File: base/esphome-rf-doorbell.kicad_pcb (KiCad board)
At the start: 2 copper layers, 65 x 54.7 mm, 100 parts, among them J1 B4B-XH, J2 CONUFL001-SMD-T, J3 Conn_01x01, J4 Conn_01x01, SW1 Boot, U1 BQ25628E, U2 RFM69W, U3 TPS7A2033, U4 MAX17261xxTD, U5 TPS629206DRLR, U6 G3VM-31DR, U7 ESP32-S2-MINI-2, U8 G3VM-63ER, U9 TLP2391

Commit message: Base board Rev3
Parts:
- removed the C1 at (130.3, 77.9)
- removed the C2 at (127.9, 77.7)
- removed C21: 0.1uF, Capacitor_SMD:C_0402_1005Metric
- removed C23: 1uF 50V, Capacitor_SMD:C_0805_2012Metric
- removed the C3 at (124.3, 81.1)
- removed the C4 at (131.6, 80.6)
- removed the C5 at (130.3, 80.2)
- removed the D3 at (114.9, 80.8)
- removed the D4 at (114.8, 78.2)
- removed J3, J4: Conn_01x01, TestPoint:TestPoint_Keystone_5000-5004_Miniature
- removed the JP1 at (118.2, 80.8)
- removed the JP2 at (118.2, 78.2)
- removed L2: 2.2uH, Inductor_SMD:L_1210_3225Metric
- removed the R1 at (111.4, 80.8)
- removed the R10 at (137.3, 96.1)
- removed the R2 at (111.4, 78.2)
- removed the R20 at (158.2, 96.9)
- removed the R21 at (158.2, 99.9)
- removed the R4 at (125.4, 94.1)
- removed the REF** at (139.5, 109.5)
- removed the REF** at (117.4, 72.1)
- removed the RV1 at (116.0, 72.9)
- removed the TP1 at (122.6, 72.9)
- removed TP11: TestPoint, TestPoint:TestPoint_Pad_D1.5mm
- removed the TP4 at (123.2, 86.9)
- removed the TP5 at (111.1, 72.9)
- removed the U7 at (125.2, 115.6)
- removed kibuzzard-691E1EB0: G***, kibuzzard-691E1EB0
- removed kibuzzard-691E1EB7: G***, kibuzzard-691E1EB7
- removed kibuzzard-691E1ECB: G***, kibuzzard-691E1ECB
- removed kibuzzard-691E1ED6: G***, kibuzzard-691E1ED6
- added C16: 1uF, Capacitor_SMD:C_0402_1005Metric, F.Cu at (138.4, 112.4)
- added C19: 1uF, Capacitor_SMD:C_0402_1005Metric, F.Cu at (148.9, 112.8)
- added C8: 47uF, Capacitor_SMD:C_0805_2012Metric, F.Cu at (132.9, 120.2)
- added D5: Red, LED_SMD:LED_0603_1608Metric, F.Cu at (142.0, 120.1)
- added JP4: SolderJumper_2_Open, Jumper:SolderJumper-2_P1.3mm_Open_RoundedPad1.0x1.5mm, F.Cu at (142.6, 117.3)
- added Q1: PMZB390UNE, Package_DFN_QFN:Diodes_DFN1006-3, F.Cu at (127.2, 106.0)
- added R12: 1.27M, Resistor_SMD:R_0402_1005Metric, F.Cu at (137.0, 112.9)
- added R16: 1k, Resistor_SMD:R_0402_1005Metric, F.Cu at (143.3, 106.6)
- added R17: 1k, Resistor_SMD:R_0402_1005Metric, F.Cu at (143.3, 113.4)
- added R18: 1k, Resistor_SMD:R_0402_1005Metric, F.Cu at (143.4, 120.1)
- added R8: 47k, Resistor_SMD:R_0402_1005Metric, F.Cu at (134.5, 106.5)
- added REF**: KiCad-Logo2_6mm_SilkScreen, Symbol:KiCad-Logo2_6mm_SilkScreen, B.Cu at (118.7, 113.4)
- added SW2: CL-SB-22A-11T, lib:CL-SB-22A, F.Cu at (164.3, 119.2)
- added U6: TPS63900, Package_SON:WSON-10-1EP_2.5x2.5mm_P0.5mm_EP1.2x2mm_ThermalVias, F.Cu at (135.8, 117.6)
- added kibuzzard-696E5F1B: G***, kibuzzard-696E5F1B, F.Cu at (168.0, 102.6)
- added kibuzzard-696E5F26: G***, kibuzzard-696E5F26, F.Cu at (167.9, 100.1)
- added kibuzzard-696E5F32: G***, kibuzzard-696E5F32, F.Cu at (167.9, 105.2)
- added kibuzzard-696E5F3B: G***, kibuzzard-696E5F3B, F.Cu at (167.9, 107.8)
- C10: value 10uF 10V -> 47uF; footprint Capacitor_SMD:C_0603_1608Metric -> Capacitor_SMD:C_0805_2012Metric
- C12: value 1uF -> 47uF; footprint Capacitor_SMD:C_0402_1005Metric -> Capacitor_SMD:C_0805_2012Metric
- C14: value 22uF 6.3V -> 1uF 25V; footprint Capacitor_SMD:C_0603_1608Metric -> Capacitor_SMD:C_0402_1005Metric
- C15: value 4.7uF -> 10uF 25V
- C6: value 4.7uF -> 100uF; footprint Capacitor_SMD:C_0603_1608Metric -> Capacitor_SMD:C_1206_3216Metric
- C7: renamed from C16; value 47nF -> 0.47uF
- C9: value 330nF -> 0.1uF
- D1: value PMEG2005EJ-QX -> BAS70; footprint Diode_SMD:D_SOD-323F -> Diode_SMD:D_SOD-523
- D3: renamed from D7; value Red -> Blue
- D6: renamed from D2; value SMBJ15CA -> SMAJ15CA; footprint Diode_SMD:D_SMB -> Diode_SMD:D_SMA
- F1: value 250mA -> 80mA; footprint Fuse:Fuse_1206_3216Metric -> Fuse:Fuse_0603_1608Metric
- J1: value B4B-XH -> PTSM 0,5/ 4-2,5-H SMD R24; footprint Connector_JST:JST_XH_B4B-XH-A_1x04_P2.50mm_Vertical -> lib:PHOENIX_1702474
- J2: value CONUFL001-SMD-T -> Conn_01x06; footprint Connector_Coaxial:U.FL_Hirose_U.FL-R-SMT-1_Vertical -> lib:Connector_PogoClamp_1.27mm; moved to B.Cu
- L1: value 1.5uH -> 2.2uH; footprint Inductor_SMD:L_Wuerth_MAPI-4020 -> Inductor_SMD:L_1210_3225Metric
- R10: renamed from R12; value 25m -> 15m; footprint Resistor_SMD:R_Shunt_Vishay_WSK2512_6332Metric_T1.19mm -> lib:R_Shunt_D1WRL1206
- R11: value 137k -> 30k; footprint Resistor_SMD:R_0603_1608Metric -> Resistor_SMD:R_0402_1005Metric
- R13: value 4.7k -> 120k
- R14: value 4.7k -> 820k; footprint Resistor_SMD:R_1206_3216Metric -> Resistor_SMD:R_0805_2012Metric
- R15: footprint Resistor_SMD:R_0603_1608Metric -> Resistor_SMD:R_0402_1005Metric
- R19: renamed from R16; value 10k -> 100k; footprint Resistor_SMD:R_0603_1608Metric -> Resistor_SMD:R_0402_1005Metric
- R2: renamed from R18; value 4.7k -> 16.9k; footprint Resistor_SMD:R_1206_3216Metric -> Resistor_SMD:R_0402_1005Metric
- R20: renamed from R22; footprint Resistor_SMD:R_0603_1608Metric -> Resistor_SMD:R_0402_1005Metric
- R21: renamed from R23; value 10k -> 100k; footprint Resistor_SMD:R_0603_1608Metric -> Resistor_SMD:R_0402_1005Metric
- R3: value 1.2k -> 100k 0.1%; footprint Resistor_SMD:R_0603_1608Metric -> Capacitor_SMD:C_0402_1005Metric
- R4: renamed from R19; value 4.7k -> 16.9k
- R5: value 13k -> 1M 0.1%; footprint Resistor_SMD:R_0402_1005Metric -> Capacitor_SMD:C_0402_1005Metric
- R6: value 30.1k -> 10k
- R7: value 10k -> 16.2k; footprint Resistor_SMD:R_0603_1608Metric -> Resistor_SMD:R_0402_1005Metric
- R9: value 619k -> 499k; footprint Resistor_SMD:R_0603_1608Metric -> Resistor_SMD:R_0402_1005Metric
- SW1: value Boot -> Flash; footprint Button_Switch_SMD:SW_SPST_PTS647_Sx50 -> Button_Switch_SMD:SW_SPST_Panasonic_EVQPL_3PL_5PL_PT_A08
- TH1: footprint Resistor_THT:R_Axial_DIN0204_L3.6mm_D1.6mm_P5.08mm_Vertical -> Resistor_SMD:R_0603_1608Metric
- TP1: renamed from TP2; footprint TestPoint:TestPoint_Keystone_5000-5004_Miniature -> TestPoint:TestPoint_Pad_D1.5mm
- TP2: renamed from TP7; footprint TestPoint:TestPoint_Keystone_5000-5004_Miniature -> TestPoint:TestPoint_Pad_D1.5mm
- TP4: renamed from TP8; moved to B.Cu
- TP5: renamed from TP9; moved to B.Cu
- TP6: renamed from TP10; moved to B.Cu
- U1: value BQ25628E -> ESP32-C6-MINI-1; footprint lib:WQFN-HR18__RYK_TEX -> lib:XCVR_ESP32-C6-MINI-1U-N4
- U2: value RFM69W -> Wio-SX1262; footprint RF_Module:HOPERF_RFM69HW -> lib:Wio-SX1262 PCB Package
- U3: value TPS7A2033 -> ISL23315; footprint Package_SON:Texas_X2SON-4_1x1mm_P0.65mm -> lib:L10_2P1X1P6A_INR
- U4: value MAX17261xxTD -> MAX17260
- U5: value TPS629206DRLR -> LTC4079; footprint lib:SOT5X3-8_DRL_TEX -> Package_DFN_QFN:DFN-10-1EP_3x3mm_P0.5mm_EP1.65x2.38mm
- U9: value TLP2391 -> LTV-354T; footprint lib:OPTO_TLP2367_TPR_E -> Package_SO:SO-4_4.4x3.6mm_P2.54mm
- moved J2 52.5 mm to (118.6, 98.3), turned to 90 degrees
- moved D6 47.8 mm to (163.8, 114.8)
- moved F1 46.0 mm to (156.4, 119.3), turned to 180 degrees
- moved C6 43.4 mm to (129.7, 119.3), turned to -90 degrees
- moved TP3 41.5 mm to (152.8, 119.5)
- moved J1 38.5 mm to (166.8, 109.2), turned to 90 degrees
- moved C10 37.6 mm to (135.8, 115.1), turned to 180 degrees
- moved RV1 37.3 mm to (156.3, 115.6)
- moved REF** 36.1 mm to (118.7, 107.0)
- moved C4 35.7 mm to (110.4, 110.6)
- moved R5 35.5 mm to (129.2, 104.3), turned to 180 degrees
- moved C9 34.6 mm to (135.4, 103.8), turned to 90 degrees
- moved C5 33.9 mm to (110.4, 113.1), turned to -90 degrees
- moved U2 33.5 mm to (122.9, 109.9), turned to 180 degrees
- moved R3 32.4 mm to (127.2, 104.3), turned to 180 degrees
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- renumbered C20 to C1, C22 to C17, C19 to C2, C17 to C3, C8 to C4, C7 to C5, D5 to D2, D6 to D4, FID3 to FID2, FID2 to FID3, JP3 to JP1, JP5 to JP2, JP4 to JP3, R8 to R1, R17 to R22, R24 to R23, RV2 to RV1, TP6 to TP3, U8 to U7, U6 to U8
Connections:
- net /BAT- renamed -BATT
- C1 pad 1: +3.3VP -> +3.3V
- C10 pad 1: GND -> +BATT
- C10 pad 2: +BATT -> GND
- C11 pad 1: VBUS -> +3.3V
- C12 pad 1: +3.3VA -> +3.3V
- C14 pad 1: +3.3VP -> VBUS
- C2 pad 1: +3.3VP -> +3.3V
- C3 pad 1: Net-(U7-EN) -> Net-(U1-EN)
- C4 pad 1: +3.3VA -> +3.3V
- C5 pad 1: +3.3VA -> +3.3V
- C6 pad 1: Net-(U1-REGN) -> +3.3V
- C9 pad 1: GND -> +3.3V
- C9 pad 2: Net-(C9-Pad2) -> GND
- D1 pad 1: /VIN -> /CHG_EN
- D2 pad 2: Net-(D5-A) -> Net-(D2-A)
- D4 pad 1: /~{BELL_SIGNAL} -> Net-(D4-K)
- D6 pad 2: Net-(D1-A) -> /I
- F1 pad 1: /I -> Net-(F1-Pad1)
- F1 pad 2: Net-(D1-A) -> VBUS
- J1 pad 1: /I -> /S_OUT
- J1 pad 2: GND -> /S_IN
- J1 pad 3: /S_IN -> /I
- J1 pad 4: /S_OUT -> GND
- J2 pad 1: /RF.Antenna -> /UART_TX
- J2 pad 2: GND -> /UART_RX
- JP3 pad 1: Net-(JP4-A) -> Net-(D4-K)
- JP3 pad 2: +3.3VP -> GND
- L1 pad 1: /SW -> Net-(U6-LX1)
- L1 pad 2: VBUS -> Net-(U6-LX2)
- R1 pad 1: +3.3VP -> +3.3V
- R1 pad 2: Net-(U7-EN) -> Net-(U1-EN)
- R11 pad 1: Net-(U5-FB/VSET) -> Net-(U5-PROG)
- R13 pad 1: +3.3VP -> /CHG_EN
- R13 pad 2: /SCL2 -> Net-(U3-RW)
- R14 pad 1: +3.3VP -> VBUS
- R14 pad 2: /SDA2 -> /CHG_EN
- R15 pad 1: Net-(D5-A) -> /OPEN_BUZZER
- R15 pad 2: /OPEN_BUZZER -> Net-(D2-A)
- R2 pad 1: +3.3VP -> +3.3V
- R2 pad 2: /SDA1 -> /SCL
- R20 pad 1: +3.3VP -> Net-(R17-Pad1)
- R20 pad 2: /~{BELL_SIGNAL} -> /BELL_SIGNAL
- R3 pad 1: Net-(C9-Pad2) -> Net-(U1-IO0)
- R3 pad 2: Net-(U1-ILIM) -> Net-(Q1-D)
- R4 pad 1: +3.3VP -> +3.3V
- R4 pad 2: /SCL1 -> /SDA
- R5 pad 1: GND -> VBUS
- R5 pad 2: Net-(R5-Pad2) -> Net-(U1-IO0)
- R6 pad 1: GND -> Net-(U5-NTCBIAS)
- R7 pad 1: /~{CE} -> Net-(U6-CFG3)
- R9 pad 1: +3.3VP -> Net-(U5-FB)
- R9 pad 2: Net-(U5-FB/VSET) -> Net-(U5-FBG)
- RV1 pad 1: Net-(C23-Pad1) -> /S_IN
- RV1 pad 2: Net-(U9-K) -> Net-(RV1-Pad2)
- RV1 pad 3: Net-(U9-K) -> Net-(RV1-Pad2)
- SW1 pad 2: Net-(U7-IO0) -> Net-(U1-IO9)
- TP1 pad 1: +3.3VP -> +3.3V
- TP3 pad 1: /VIN -> VBUS
- TP4 pad 1: /~{BELL_SIGNAL} -> /BELL_SIGNAL
- U1 pad 1: /BTST -> GND
- U1 pad 10: Net-(JP1-A) -> /BELL_OFF
- U1 pad 11: /~{INT} -> GND
- U1 pad 12: /SDA1 -> Net-(U1-IO0)
- U1 pad 13: /SCL1 -> /V_{PROG}
- U1 pad 14: /~{CE} -> GND
- U1 pad 15: GND -> Net-(Q1-G)
- U1 pad 16: /SW -> Net-(D1-A)
- U1 pad 17: Net-(U1-PMID) -> /SCL
- U1 pad 18: /VIN -> /SDA
- U1 pad 2: Net-(U1-REGN) -> GND
- U1 pad 3: Net-(JP2-A) -> +3.3V
- U1 pad 4: Net-(U1-ILIM) -> unconnected-(U1-NC-Pad4)
- U1 pad 5: Net-(U1-TS_BIAS) -> /BAT_ALERT
- U1 pad 6: /TH -> /RF_DIO1
- U1 pad 8: +BATT -> Net-(U1-EN)
- U1 pad 9: VBUS -> /BELL_SIGNAL
- U2 pad 1: /RF.Reset -> unconnected-(U2-RF_SW1-Pad1)
- U2 pad 10: /RF.Antenna -> GND
- U2 pad 11: GND -> /RF_BUSY
- U2 pad 12: /RF.SCLK -> /RF_DIO1
- U2 pad 2: /RF.IO0 -> /SPI_MISO
- U2 pad 3: /RF.IO1 -> /SPI_MOSI
- U2 pad 4: /RF.IO2 -> /SPI_CLK
- U2 pad 5: /RF.IO3 -> /RF_RST
- U2 pad 6: /RF.IO4 -> /~{CS_RF}
- U2 pad 7: /RF.IO5 -> GND
- U2 pad 8: +3.3VA -> +3.3V
- U2 pad 9: GND -> unconnected-(U2-ANT-Pad9)
- U3 pad 1: +3.3VA -> /SCL
- U3 pad 2: GND -> /SDA
- U3 pad 3: /RF_PWR_EN -> GND
- U3 pad 4: VBUS -> GND
- U4 pad 13: /SDA2 -> /SDA
- U4 pad 14: /SCL2 -> /SCL
- U5 pad 1: Net-(U5-FB/VSET) -> VBUS
- U5 pad 2: unconnected-(U5-PG-Pad2) -> /CHG_EN
- U5 pad 3: +3.3VP -> Net-(U5-PROG)
- U5 pad 4: Net-(U5-SW) -> Net-(U5-NTCBIAS)
- U5 pad 5: GND -> /TH
- U5 pad 6: VBUS -> GND
- U5 pad 7: VBUS -> Net-(JP4-A)
- U5 pad 8: Net-(U5-MODE) -> Net-(U5-FBG)
- U9 pad 3: Net-(U9-K) -> Net-(R17-Pad1)
- U9 pad 4: GND -> +3.3V
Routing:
- net +3.3VP: track 118.3 -> 0.00 mm, vias 10 -> 0
- net +3.3V: track 0.00 -> 105.9 mm, vias 0 -> 15
- net /~{BELL_SIGNAL}: track 62.8 -> 0.00 mm
- net /BELL_SIGNAL: track 0.00 -> 47.6 mm, vias 0 -> 2
- net /RF.SCLK: track 39.1 -> 0.00 mm
- net /RF.MISO: track 38.3 -> 0.00 mm
- net /RF.MOSI: track 37.4 -> 0.00 mm
- net /RF.CE: track 36.6 -> 0.00 mm
- net /~{CE}: track 36.2 -> 0.00 mm, vias 2 -> 0
- net /DC_EN: track 0.00 -> 34.6 mm, vias 0 -> 2
- net /~{INT}: track 33.5 -> 0.00 mm
- net /SDA1: track 33.3 -> 0.00 mm
- net /SCL1: track 33.1 -> 0.00 mm
- net /SCL: track 0.00 -> 32.9 mm, vias 0 -> 5
- net VBUS: track 67.7 -> 36.9 mm, vias 5 -> 4
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- added copper zone on F.Cu, net +3.3V
- added copper zone on In2.Cu, net +3.3V
- added copper zone on In1.Cu, net GND
- added copper zone on In2.Cu, net GND
- added copper zone on F.Cu, net Net-(U6-LX1)
- added copper zone on F.Cu, net Net-(U6-LX2)
- removed copper zone on F.Cu, net /BTST
- removed copper zone on F.Cu, net /SW
- removed copper zone on F.Cu, net /VIN
- removed copper zone on F.Cu, net Net-(U5-SW)
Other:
- board size 65 x 54.7 mm -> 59.9 x 25.8 mm
- copper layers 2 -> 4
- board text added: "3.3V"
- board text added: "BELL"
- board text added: "RXD"
- board text added: "SCL"
- board text added: "SDA"
- board text added: "Smart doorbell with remote for Homeassistant https://github.com/usimd/esphome-rf-doorbell, Rev ${Revision}"
- board text added: "TXD"
- board text added: "VBUS"
- board text removed: "+3.3V (ESP)"
- board text removed: "113kΩ"
- board text removed: "13kΩ"
- board text removed: "192mA"
- board text removed: "22.1mA"
- board text removed: "BOOT"
- board text removed: "I_{CHG}"
- board text removed: "PG"
- board text removed: "RX"
- board text removed: "R_{ISET}"
- board text removed: "STAT"
- board text removed: "Smart doorbell for STR HT2001 with remote for Homeassistant https://github.com/usimd/esphome-rf-doorbell, Rev ${Revision}"
- board text removed: "TX"
- board text removed: "VIN"
- board text removed: "~{BELL}"

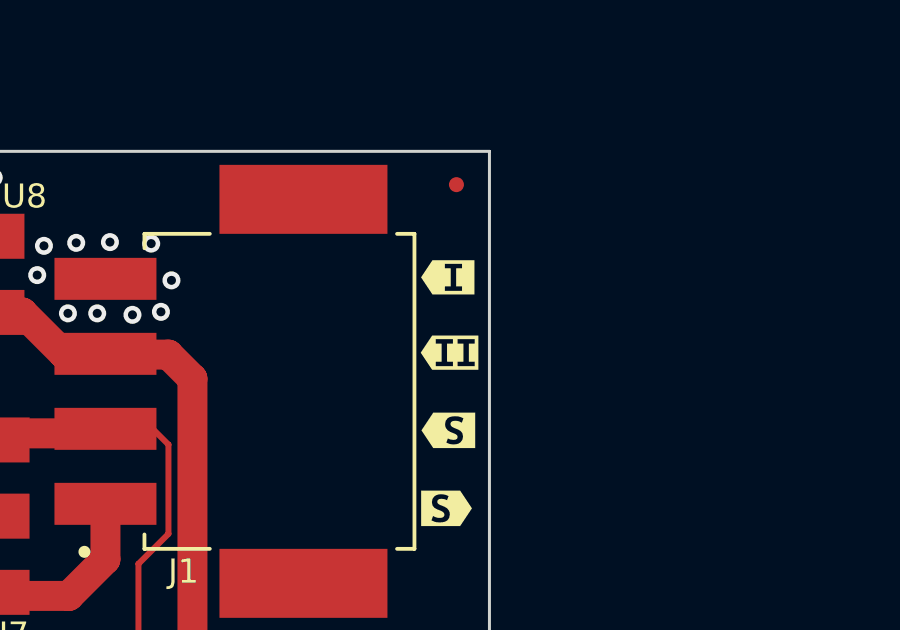
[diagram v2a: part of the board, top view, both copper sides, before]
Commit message: Update docs, fix fuel gauge issue
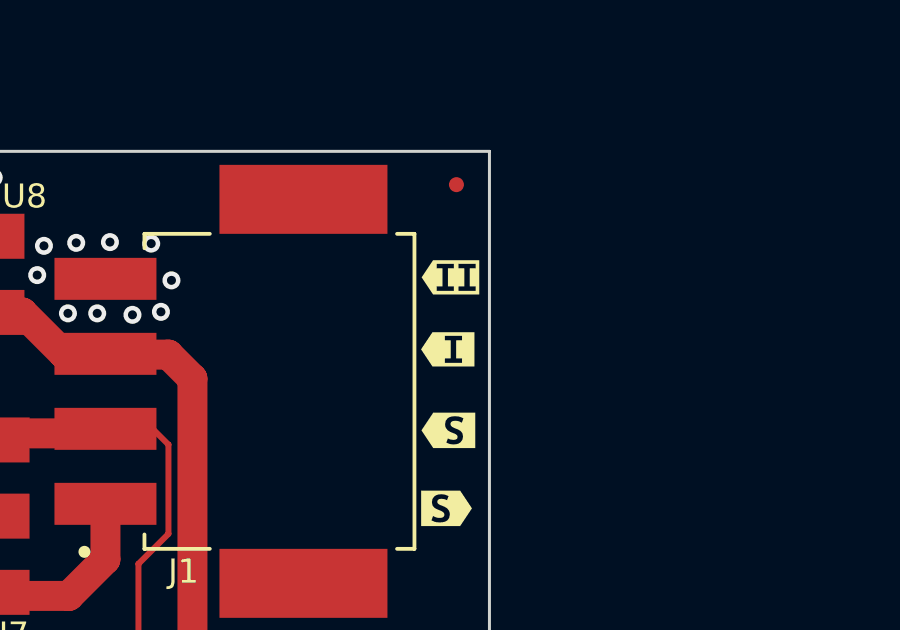
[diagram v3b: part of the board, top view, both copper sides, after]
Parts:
- moved kibuzzard-696E5F1B 2.51 mm to (168.0, 100.1)
- moved kibuzzard-696E5F26 2.40 mm to (167.9, 102.5)

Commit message: Rev 4
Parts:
- removed REF**: KiCad-Logo2_6mm_SilkScreen, Symbol:KiCad-Logo2_6mm_SilkScreen
- removed REF**: OSHW-Logo2_7.3x6mm_SilkScreen, Symbol:OSHW-Logo2_7.3x6mm_SilkScreen
- added R24: 47k, Capacitor_SMD:C_0402_1005Metric, F.Cu at (125.6, 103.6)
- added R25: 0, Capacitor_SMD:C_0402_1005Metric, F.Cu at (123.7, 116.0)
- added R26: 100k, Capacitor_SMD:C_0402_1005Metric, F.Cu at (124.7, 116.0)
- R11: value 30k -> 20k
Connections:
- U1 pad 20: unconnected-(U1-IO15-Pad20) -> /RF_SWITCH
- U1 pad 22: unconnected-(U1-IO8-Pad22) -> Net-(U1-IO8)
- U2 pad 1: unconnected-(U2-RF_SW1-Pad1) -> Net-(U2-RF_SW1)
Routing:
- net /RF_SWITCH: track 0.00 -> 12.8 mm, vias 0 -> 2
- net +3.3V: track 105.9 -> 113.3 mm, vias 15 -> 16
- net Net-(U1-IO8): track 0.00 -> 6.57 mm, vias 0 -> 2
- net Net-(U2-RF_SW1): track 0.00 -> 6.40 mm, vias 0 -> 2
- net GND: vias 168 -> 166
